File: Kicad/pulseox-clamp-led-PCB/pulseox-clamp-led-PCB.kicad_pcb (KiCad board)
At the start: 2 copper layers, 10 x 8 mm, 5 parts, among them P1 Header 3

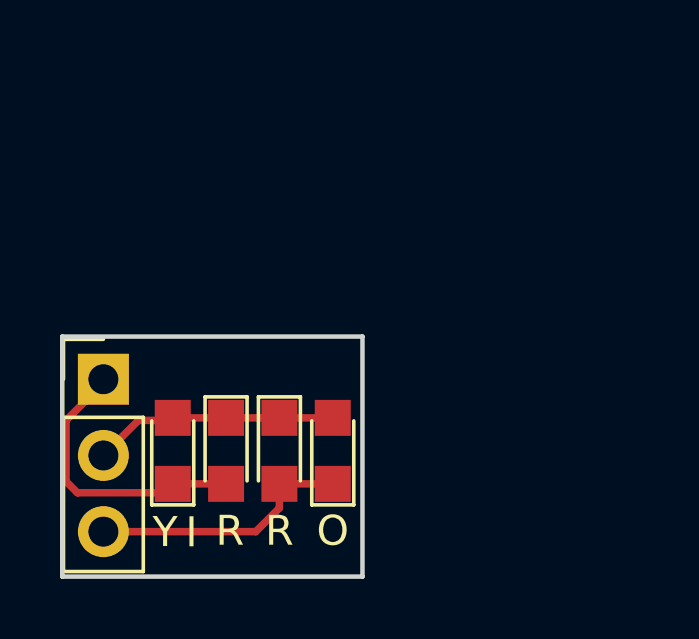
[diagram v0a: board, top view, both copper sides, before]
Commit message: Added output PDF files from Kicad project
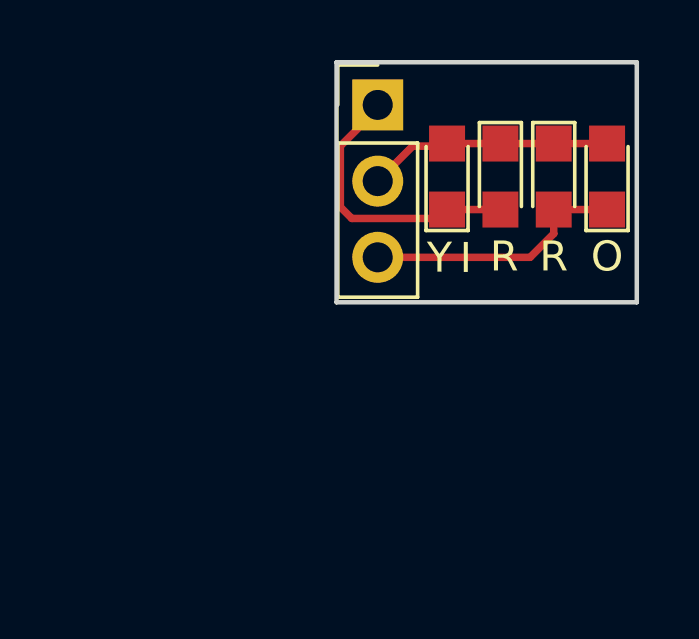
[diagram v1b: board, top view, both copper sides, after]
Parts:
- moved O 12.9 mm to (154.6, 97.3)
- moved R 12.9 mm to (152.8, 97.3)
- moved Y 12.9 mm to (149.2, 97.3)
- moved P1 12.9 mm to (146.9, 94.9)
- moved I 12.9 mm to (151.0, 97.3)
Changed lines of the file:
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@@
     (links 8)
     (no_connects 0)
-    (area 136.322999 102.540999 146.480601 110.692001)
+    (area 134.117219 100.7334 148.04 112.5234)
     (thickness 1.6)
-    (drawings 5)
+    (drawings 7)
     (tracks 17)
     (zones 0)
@@
   )
   (page A4)
+  (title_block
+    (title pulseox-clamp-led-pcb)
+    (date 2018-07-18)
+    (rev 2.1)
+    (company IRNAS)
+  )
   (layers
     (0 F.Cu signal)
@@
   )
   (module LEDs:LED_0805 (layer F.Cu)
-    (at 140.081 106.426 90)
+    (at 149.225 97.282 90)
     (descr "LED 0805 smd package")
     (tags "LED led 0805 SMD smd SMT smt smdled SMDLED smtled SMTLED")
@@
   )
   (module LEDs:LED_0805 (layer F.Cu)
-    (at 143.637 106.426 270)
+    (at 152.781 97.282 270)
     (descr "LED 0805 smd package")
     (tags "LED led 0805 SMD smd SMT smt smdled SMDLED smtled SMTLED")
@@
   )
   (module LEDs:LED_0805 (layer F.Cu)
-    (at 141.859 106.426 270)
+    (at 151.003 97.282 270)
     (descr "LED 0805 smd package")
     (tags "LED led 0805 SMD smd SMT smt smdled SMDLED smtled SMTLED")
@@
   )
   (module LEDs:LED_0805 (layer F.Cu)
-    (at 145.415 106.426 90)
+    (at 154.559 97.282 90)
     (descr "LED 0805 smd package")
     (tags "LED led 0805 SMD smd SMT smt smdled SMDLED smtled SMTLED")
@@
   )
   (module Pin_Headers:Pin_Header_Straight_1x03_Pitch2.54mm (layer F.Cu)
-    (at 137.7696 104.0384)
+    (at 146.9136 94.8944)
     (descr "Through hole straight pin header, 1x03, 2.54mm pitch, single row")
     (tags "Through hole pin header THT 1x03 2.54mm single row")
@@
     )
   )
-  (gr_line (start 146.4056 102.616) (end 146.4056 110.617) (angle 90) (layer Edge.Cuts) (width 0.15))
-  (gr_line (start 136.398 102.616) (end 146.4056 102.616) (angle 90) (layer Edge.Cuts) (width 0.15))
-  (gr_line (start 136.398 110.617) (end 146.4056 110.617) (angle 90) (layer Edge.Cuts) (width 0.15))
-  (gr_text R (at 143.637 109.093) (layer F.SilkS)
+  (dimension 8.001 (width 0.25) (layer Dwgs.User)
+    (gr_text "8,00 mm" (at 160.3032 97.4725 270) (layer Dwgs.User)
+      (effects (font (size 1 1) (thickness 0.25)))
+    )
+    (feature1 (pts (xy 155.5496 101.473) (xy 161.6532 101.473)))
+    (feature2 (pts (xy 155.5496 93.472) (xy 161.6532 93.472)))
+    (crossbar (pts (xy 158.9532 93.472) (xy 158.9532 101.473)))
+    (arrow1a (pts (xy 158.9532 101.473) (xy 158.366779 100.346496)))
+    (arrow1b (pts (xy 158.9532 101.473) (xy 159.539621 100.346496)))
+    (arrow2a (pts (xy 158.9532 93.472) (xy 158.366779 94.598504)))
+    (arrow2b (pts (xy 158.9532 93.472) (xy 159.539621 94.598504)))
+  )
+  (dimension 10.0076 (width 0.25) (layer Dwgs.User)
+    (gr_text "10,00 mm" (at 150.8252 90.5002) (layer Dwgs.User)
+      (effects (font (size 1 1) (thickness 0.25)))
+    )
+    (feature1 (pts (xy 155.5496 93.472) (xy 155.5496 89.3242)))
+    (feature2 (pts (xy 145.542 93.472) (xy 145.542 89.3242)))
+    (crossbar (pts (xy 145.542 92.0242) (xy 155.5496 92.0242)))
+    (arrow1a (pts (xy 155.5496 92.0242) (xy 154.423096 92.610621)))
+    (arrow1b (pts (xy 155.5496 92.0242) (xy 154.423096 91.437779)))
+    (arrow2a (pts (xy 145.542 92.0242) (xy 146.668504 92.610621)))
+    (arrow2b (pts (xy 145.542 92.0242) (xy 146.668504 91.437779)))
+  )
+  (gr_line (start 155.5496 93.472) (end 155.5496 101.473) (angle 90) (layer Edge.Cuts) (width 0.15))
+  (gr_line (start 145.542 93.472) (end 155.5496 93.472) (angle 90) (layer Edge.Cuts) (width 0.15))
+  (gr_line (start 145.542 101.473) (end 155.5496 101.473) (angle 90) (layer Edge.Cuts) (width 0.15))
+  (gr_text R (at 152.781 99.949) (layer F.SilkS)
     (effects (font (size 1 1) (thickness 0.15)))
   )
-  (gr_line (start 136.398 102.616) (end 136.398 110.616) (angle 90) (layer Edge.Cuts) (width 0.15))
-  (segment (start 143.637 105.326) (end 145.415 105.326) (width 0.25) (layer F.Cu) (net 1) (status C00000))
-  (segment (start 141.859 105.326) (end 143.637 105.326) (width 0.25) (layer F.Cu) (net 1) (status C00000))
-  (segment (start 140.081 105.326) (end 141.859 105.326) (width 0.25) (layer F.Cu) (net 1) (status C00000))
-  (segment (start 137.7696 106.5784) (end 138.938 105.41) (width 0.25) (layer F.Cu) (net 1) (status 400000))
-  (segment (start 138.938 105.41) (end 139.997 105.41) (width 0.25) (layer F.Cu) (net 1) (status 800000))
-  (segment (start 139.997 105.41) (end 140.081 105.326) (width 0.25) (layer F.Cu) (net 1) (status C00000))
-  (segment (start 140.081 107.526) (end 141.859 107.526) (width 0.25) (layer F.Cu) (net 2) (status C00000))
-  (segment (start 137.7696 104.0384) (end 137.7696 104.1654) (width 0.25) (layer F.Cu) (net 2) (status C00000))
-  (segment (start 137.7696 104.1654) (end 136.525 105.41) (width 0.25) (layer F.Cu) (net 2) (status 400000))
-  (segment (start 136.525 105.41) (end 136.525 107.442) (width 0.25) (layer F.Cu) (net 2))
-  (segment (start 136.525 107.442) (end 136.906 107.823) (width 0.25) (layer F.Cu) (net 2))
-  (segment (start 136.906 107.823) (end 139.784 107.823) (width 0.25) (layer F.Cu) (net 2) (status 800000))
-  (segment (start 139.784 107.823) (end 140.081 107.526) (width 0.25) (layer F.Cu) (net 2) (status C00000))
-  (segment (start 143.637 107.526) (end 143.637 108.331) (width 0.25) (layer F.Cu) (net 3) (status 400000))
-  (segment (start 142.8496 109.1184) (end 137.7696 109.1184) (width 0.25) (layer F.Cu) (net 3) (status 800000))
-  (segment (start 143.637 108.331) (end 142.8496 109.1184) (width 0.25) (layer F.Cu) (net 3))
-  (segment (start 145.415 107.526) (end 143.637 107.526) (width 0.25) (layer F.Cu) (net 3) (status C00000))
+  (gr_line (start 145.542 93.472) (end 145.542 101.472) (angle 90) (layer Edge.Cuts) (width 0.15))
+  (segment (start 152.781 96.182) (end 154.559 96.182) (width 0.25) (layer F.Cu) (net 1))
+  (segment (start 151.003 96.182) (end 152.781 96.182) (width 0.25) (layer F.Cu) (net 1))
+  (segment (start 149.225 96.182) (end 151.003 96.182) (width 0.25) (layer F.Cu) (net 1))
+  (segment (start 146.9136 97.4344) (end 148.082 96.266) (width 0.25) (layer F.Cu) (net 1))
+  (segment (start 148.082 96.266) (end 149.141 96.266) (width 0.25) (layer F.Cu) (net 1))
+  (segment (start 149.141 96.266) (end 149.225 96.182) (width 0.25) (layer F.Cu) (net 1))
+  (segment (start 149.225 98.382) (end 151.003 98.382) (width 0.25) (layer F.Cu) (net 2))
+  (segment (start 146.9136 94.8944) (end 146.9136 95.0214) (width 0.25) (layer F.Cu) (net 2))
+  (segment (start 146.9136 95.0214) (end 145.669 96.266) (width 0.25) (layer F.Cu) (net 2))
+  (segment (start 145.669 96.266) (end 145.669 98.298) (width 0.25) (layer F.Cu) (net 2))
+  (segment (start 145.669 98.298) (end 146.05 98.679) (width 0.25) (layer F.Cu) (net 2))
+  (segment (start 146.05 98.679) (end 148.928 98.679) (width 0.25) (layer F.Cu) (net 2))
+  (segment (start 148.928 98.679) (end 149.225 98.382) (width 0.25) (layer F.Cu) (net 2))
+  (segment (start 152.781 98.382) (end 152.781 99.187) (width 0.25) (layer F.Cu) (net 3))
+  (segment (start 151.9936 99.9744) (end 146.9136 99.9744) (width 0.25) (layer F.Cu) (net 3))
+  (segment (start 152.781 99.187) (end 151.9936 99.9744) (width 0.25) (layer F.Cu) (net 3))
+  (segment (start 154.559 98.382) (end 152.781 98.382) (width 0.25) (layer F.Cu) (net 3))
 )
